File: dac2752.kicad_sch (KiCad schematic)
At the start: 30 parts, among them U30 LTC2752B, U301 OPA2197D, U31 OPA2189DGK, U32 OPA2388DGK

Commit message: Everything assigned except for wierd shit.
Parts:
- added C305, C314, C315: 0u1, Capacitor_SMD:C_0402_1005Metric, symbol Device:C
- added NT31: NetTie_2, symbol Device:NetTie_2
- added TP301, TP302, TP303, TP304: TestPoint, Parts:TestPoint, symbol Connector:TestPoint
- added U305: DG419D, Package_SO:SOIC-8_3.9x4.9mm_P1.27mm, symbol Parts:DG419
- C301, C304: value 0n1 -> 330p; LCSC (none) -> C1664; now fitted; now in the parts list
- R301, R309: value 33 -> 100
- R302, R310: value 33k -> 100k
- R315: LCSC (none) -> C25076
- U30: LCSC (none) -> C682625
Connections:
- net +18V: now also C314.1, U305.4 (VDD)
- net -18V: now also C315.2, U305.7 (VSS)
- net GND: now also NT31.1, U305.8 (S2); no longer R305.2, R306.1, R309.2, U30.8 (IOUT2AS), U30.9 (IOUT2AF)
- net GNDPWR: now also C305.2, C314.2, C315.1, U305.3 (GND)
- net Out: now also U305.1 (D); no longer U30.46 (RFBA)
- net at C306.1, R313.1, R314.1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: now also TP304.1
- net at C303.1, R313.2, R314.2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: now also TP303.1
- net at R307.1, R308.1, U30.47 (ROFSA)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: now also TP302.1
- net at C313.1, R307.2, R308.2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: now also TP301.1
- new net: U30.46 (RFBA), U305.2 (S1)
- new net: NT31.2, R305.2, R306.1, R309.2, U30.8 (IOUT2AS), U30.9 (IOUT2AF)
- new net +3V3A: C305.1, U305.5 (V_{L})
- new net Select: U305.6 (SEL)
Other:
- moved on the sheet: C302, C303, C306, C307, C308, C309, C310, C311, C313, R301, R302, R303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

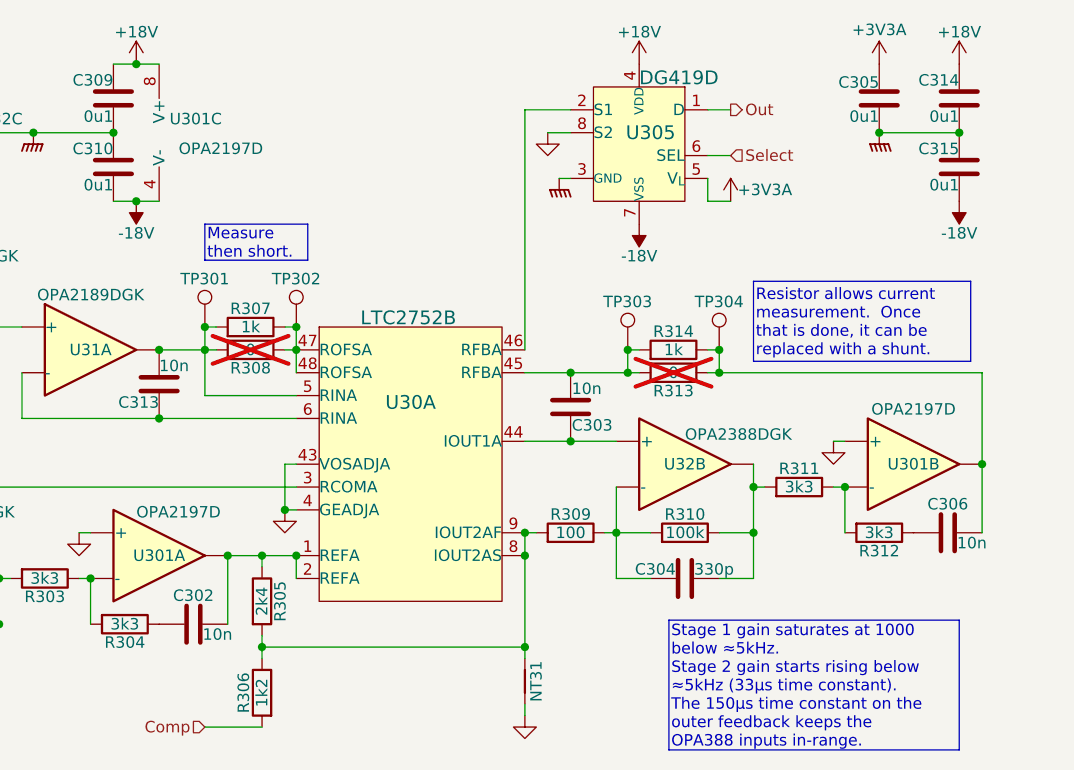
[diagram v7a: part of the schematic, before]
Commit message: Layout underway
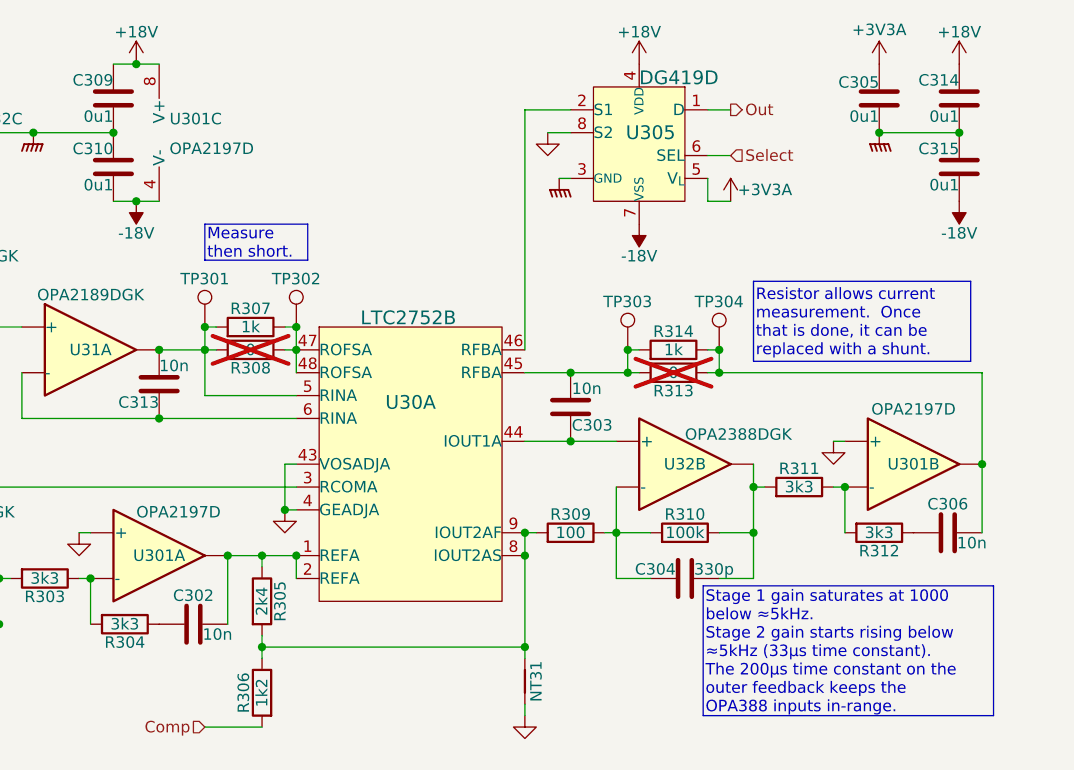
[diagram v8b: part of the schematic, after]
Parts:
- NT31: footprint (none) -> NetTie:NetTie-2_SMD_Pad0.5mm; symbol Device:NetTie_2 -> Parts:NetTie_2
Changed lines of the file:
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@@
 		)
 	)
-	(text_box "Stage 1 gain saturates at 1000 below ≈5kHz.\nStage 2 gain starts rising below ≈5kHz (33µs time constant).\nThe 150µs time constant on the outer feedback keeps the OPA388 inputs in-range."
+	(text_box "Stage 1 gain saturates at 1000 below ≈5kHz.\nStage 2 gain starts rising below ≈5kHz (33µs time constant).\nThe 200µs time constant on the outer feedback keeps the OPA388 inputs in-range."
 		(exclude_from_sim no)
-		(at 151.8919 108.7699 0)
+		(at 155.7019 104.9599 0)
 		(size 32.2581 14.4201)
 		(margins 0.254 0.254 0.254 0.254)
@@
 		)
 		(property "Value" "OPA2197D"
-			(at 102.108 56.388 0)
+			(at 101.092 56.388 0)
 			(effects
 				(font
@@
 	)
 	(symbol
-		(lib_id "Device:NetTie_2")
+		(lib_id "Parts:NetTie_2")
 		(at 135.89 115.57 270)
 		(mirror x)
@@
 			)
 		)
-		(property "Footprint" ""
+		(property "Footprint" "NetTie:NetTie-2_SMD_Pad0.5mm"
 			(at 135.89 115.57 0)
 			(effects
